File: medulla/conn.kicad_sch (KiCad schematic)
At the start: 1 part, among them J1 ESQ-120-XX-X-D-XX

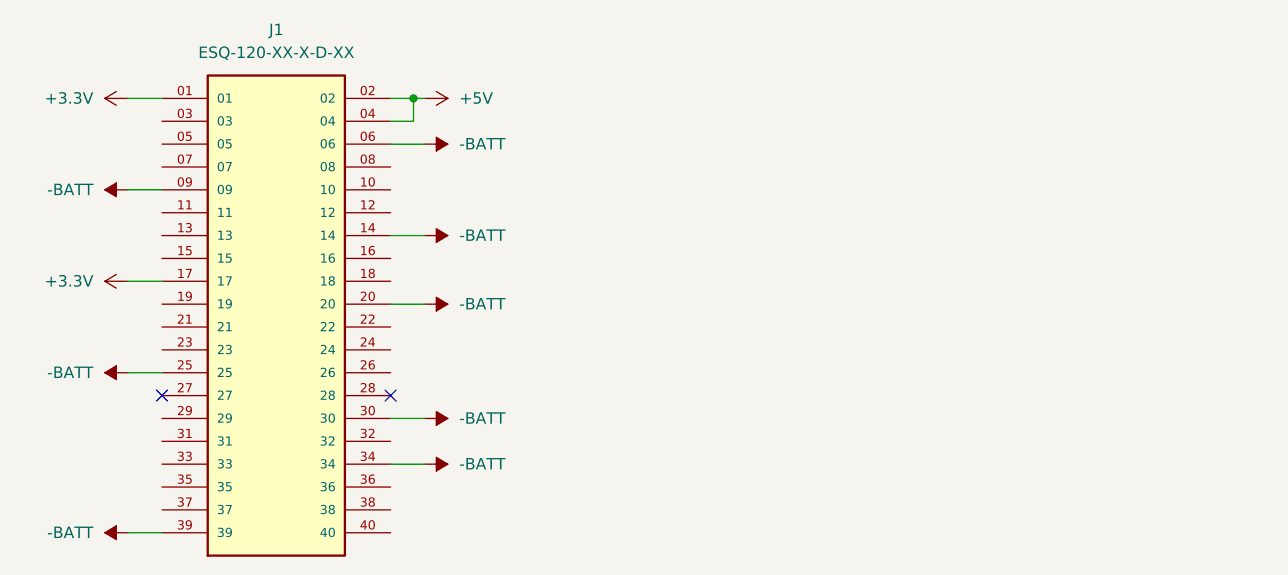
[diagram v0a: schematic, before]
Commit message: 0.1.3-alpha: H-Bridge Completion & I2C Sensor integration
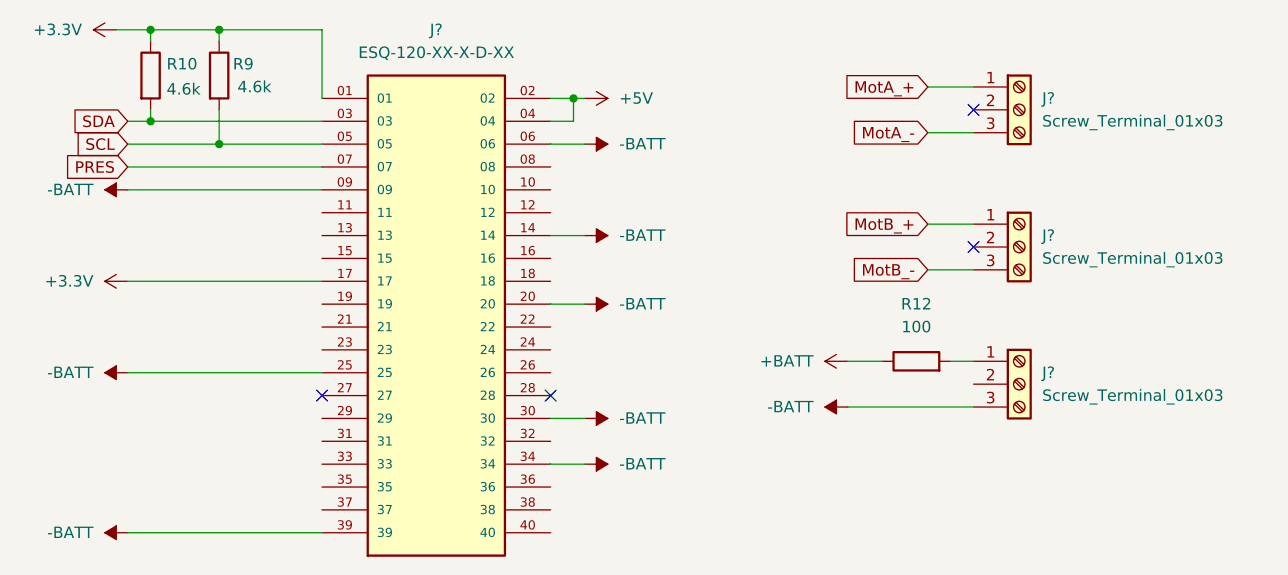
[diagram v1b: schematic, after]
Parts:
- added J? (x3): Screw_Terminal_01x03, symbol Connector:Screw_Terminal_01x03
- added R10, R9: 4.6k, symbol Device:R
- added R12: 100, symbol Device:R
- renumbered J1 to J?
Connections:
- net +3.3V: now also R10.1, R9.1
- net -BATT: now also J?.3 (Pin_3)
- net SDA: now reaches J?.03
- net SDA: now also R10.2
- net SCL: now reaches J?.05
- net SCL: now also R9.2
- net PRES: now reaches J?.07
- new net: J?.1 (Pin_1), R12.2
- new net +BATT: R12.1
- new net MotA_+: J?.1 (Pin_1)
- new net MotA_-: J?.3 (Pin_3)
- new net MotB_+: J?.1 (Pin_1)
- new net MotB_-: J?.3 (Pin_3)
- no-connect marks 2 -> 4
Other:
- moved on the sheet: J?
